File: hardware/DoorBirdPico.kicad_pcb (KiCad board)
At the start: 2 copper layers, 62 x 73.7 mm, 41 parts, among them J0 Doorbird, J1 Reed, J10 Taste A, J20 Taste B, J3 Relay_Opener, J30 Taste C, J4 Relais_in, J40 RS485, J98 Conn_01x20, J99 Conn_01x20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

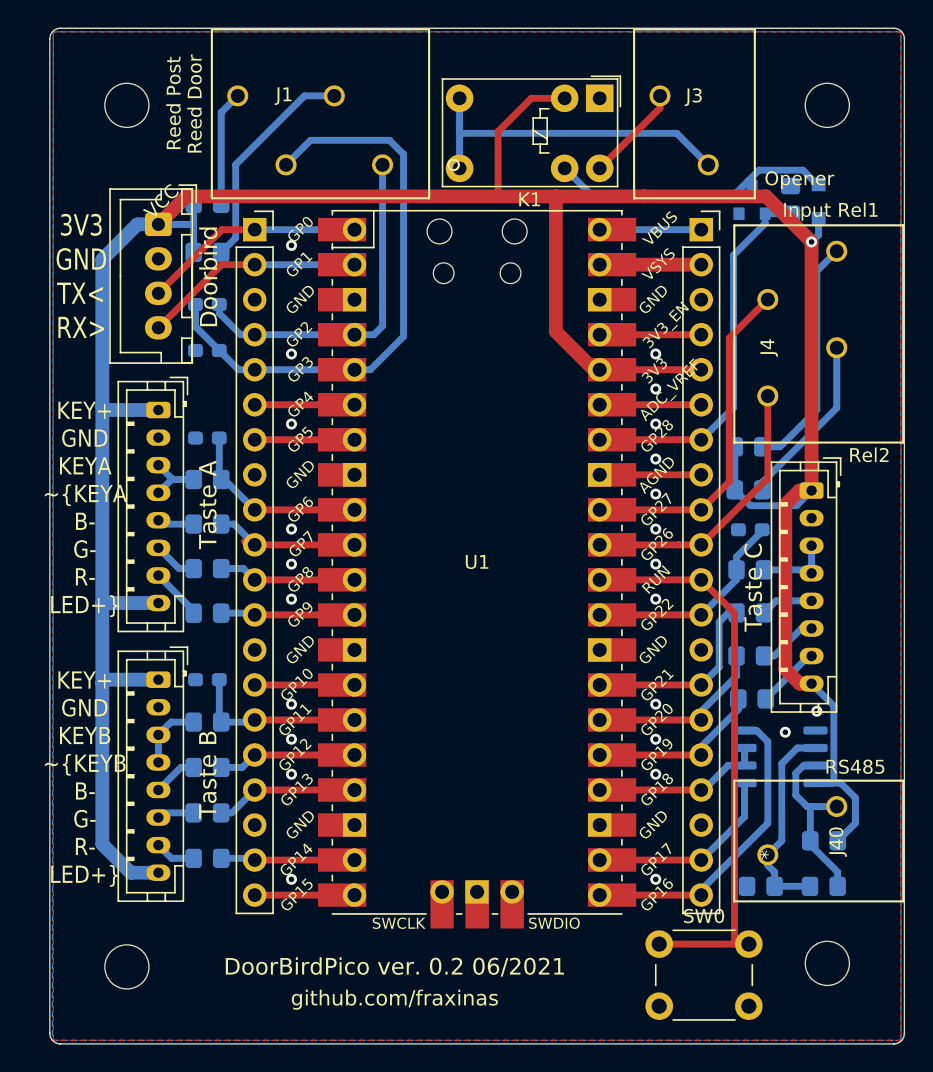
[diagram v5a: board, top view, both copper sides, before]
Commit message: PCB: Add P-MOS for decoupling Doorbird VCC from USB Power
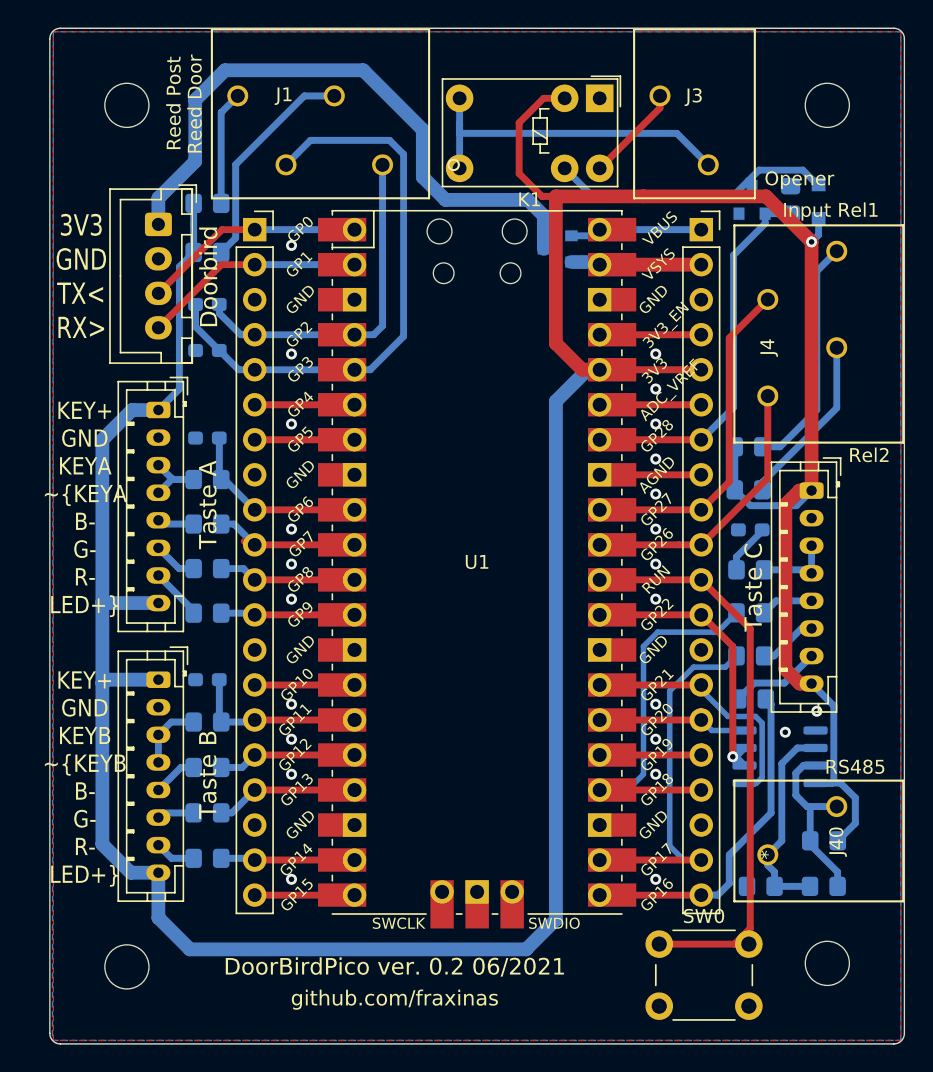
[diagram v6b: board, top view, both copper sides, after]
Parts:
- added Q2: AO3401A, Package_TO_SOT_SMD:SOT-23, B.Cu at (158.8, 57.7)
- turned R33 to 0 degrees
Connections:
- C30 pad 1: GND -> (no net)
- J0 pad 1: +3V3 -> Net-(J0-Pad1)
- J98 pad 12: Net-(C30-Pad2) -> Net-(J98-Pad12)
- R31 pad 2: Net-(J98-Pad14) -> Net-(J98-Pad17)
- R32 pad 2: Net-(J98-Pad15) -> Net-(J98-Pad19)
- R33 pad 2: Net-(J98-Pad16) -> Net-(J98-Pad20)
- U1 pad 29: Net-(C30-Pad2) -> Net-(J98-Pad12)
- U40 pad 1: Net-(J98-Pad19) -> Net-(J98-Pad14)
- U40 pad 2: Net-(J98-Pad17) -> Net-(J98-Pad12)
- U40 pad 3: Net-(J98-Pad17) -> Net-(J98-Pad12)
- U40 pad 4: Net-(J98-Pad20) -> Net-(J98-Pad15)
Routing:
- net Net-(J0-Pad1): track 0.00 -> 45.1 mm
- net +3V3: track 215.4 -> 254.9 mm
- net Net-(J98-Pad12): track 0.00 -> 20.6 mm, vias 0 -> 1
- net Net-(J98-Pad17): track 12.6 -> 28.3 mm
- net Net-(J98-Pad19): track 14.3 -> 27.2 mm
- net Net-(C30-Pad2): track 15.5 -> 3.67 mm
- net Net-(J98-Pad16): track 12.6 -> 8.03 mm
- net Net-(J98-Pad14): track 14.1 -> 18.6 mm
- net Net-(J98-Pad20): track 22.5 -> 24.9 mm
- net Net-(J98-Pad1): track 7.37 -> 9.60 mm
- net Net-(J30-Pad7): track 4.61 -> 6.81 mm
- net Net-(J98-Pad2): track 7.37 -> 9.49 mm
- net Net-(J98-Pad15): track 13.1 -> 11.5 mm
- net Net-(J98-Pad11): track 41.3 -> 42.3 mm
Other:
- board text removed: "VCC"
